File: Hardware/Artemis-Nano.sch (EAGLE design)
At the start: 66 parts, among them J10 USB-C, J11 CORTEX_DEBUG, U2 MCP73831, U3 3.3V, U4 ARTEMIS_MODULESMD, U6 CH340E_MSOP10, Y2 32.768kHz

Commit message: Rename to Nano. Add ignore. Add panel.
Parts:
- removed LOGO2: OSHW-LOGOS, SparkFun-Aesthetics:OSHW-LOGOS
- removed LOGO3: SFE_LOGO_NAME_FLAME.1_INCH, SparkFun-Aesthetics:SFE_LOGO_NAME_FLAME.1_INCH
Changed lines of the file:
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@@
 <grid distance="0.1" unitdist="inch" unit="inch" style="lines" multiple="1" display="no" altdistance="0.01" altunitdist="inch" altunit="inch"/>
 <layers>
-<layer number="1" name="Top" color="4" fill="1" visible="yes" active="no"/>
-<layer number="2" name="Route2" color="16" fill="3" visible="yes" active="no"/>
-<layer number="3" name="Route3" color="4" fill="3" visible="yes" active="no"/>
-<layer number="4" name="Route4" color="1" fill="4" visible="yes" active="no"/>
-<layer number="5" name="Route5" color="4" fill="4" visible="yes" active="no"/>
-<layer number="6" name="Route6" color="1" fill="8" visible="yes" active="no"/>
-<layer number="7" name="Route7" color="4" fill="8" visible="yes" active="no"/>
-<layer number="8" name="Route8" color="1" fill="2" visible="yes" active="no"/>
-<layer number="9" name="Route9" color="4" fill="2" visible="yes" active="no"/>
-<layer number="10" name="Route10" color="1" fill="7" visible="yes" active="no"/>
-<layer number="11" name="Route11" color="4" fill="7" visible="yes" active="no"/>
-<layer number="12" name="Route12" color="1" fill="5" visible="yes" active="no"/>
-<layer number="13" name="Route13" color="4" fill="5" visible="yes" active="no"/>
-<layer number="14" name="Route14" color="1" fill="6" visible="yes" active="no"/>
-<layer number="15" name="Route15" color="23" fill="6" visible="yes" active="no"/>
-<layer number="16" name="Bottom" color="1" fill="1" visible="yes" active="no"/>
-<layer number="17" name="Pads" color="2" fill="1" visible="yes" active="no"/>
-<layer number="18" name="Vias" color="2" fill="1" visible="yes" active="no"/>
-<layer number="19" name="Unrouted" color="6" fill="1" visible="yes" active="no"/>
-<layer number="20" name="Dimension" color="24" fill="1" visible="yes" active="no"/>
-<layer number="21" name="tPlace" color="16" fill="1" visible="yes" active="no"/>
-<layer number="22" name="bPlace" color="14" fill="1" visible="yes" active="no"/>
-<layer number="23" name="tOrigins" color="15" fill="1" visible="yes" active="no"/>
-<layer number="24" name="bOrigins" color="15" fill="1" visible="yes" active="no"/>
-<layer number="25" name="tNames" color="7" fill="1" visible="yes" active="no"/>
-<layer number="26" name="bNames" color="7" fill="1" visible="yes" active="no"/>
-<layer number="27" name="tValues" color="7" fill="1" visible="yes" active="no"/>
-<layer number="28" name="bValues" color="7" fill="1" visible="yes" active="no"/>
+<layer number="1" name="Top" color="4" fill="1" visible="no" active="no"/>
+<layer number="2" name="Route2" color="16" fill="3" visible="no" active="no"/>
+<layer number="3" name="Route3" color="4" fill="3" visible="no" active="no"/>
+<layer number="4" name="Route4" color="1" fill="4" visible="no" active="no"/>
+<layer number="5" name="Route5" color="4" fill="4" visible="no" active="no"/>
+<layer number="6" name="Route6" color="1" fill="8" visible="no" active="no"/>
+<layer number="7" name="Route7" color="4" fill="8" visible="no" active="no"/>
+<layer number="8" name="Route8" color="1" fill="2" visible="no" active="no"/>
+<layer number="9" name="Route9" color="4" fill="2" visible="no" active="no"/>
+<layer number="10" name="Route10" color="1" fill="7" visible="no" active="no"/>
+<layer number="11" name="Route11" color="4" fill="7" visible="no" active="no"/>
+<layer number="12" name="Route12" color="1" fill="5" visible="no" active="no"/>
+<layer number="13" name="Route13" color="4" fill="5" visible="no" active="no"/>
+<layer number="14" name="Route14" color="1" fill="6" visible="no" active="no"/>
+<layer number="15" name="Route15" color="23" fill="6" visible="no" active="no"/>
+<layer number="16" name="Bottom" color="1" fill="1" visible="no" active="no"/>
+<layer number="17" name="Pads" color="2" fill="1" visible="no" active="no"/>
+<layer number="18" name="Vias" color="2" fill="1" visible="no" active="no"/>
+<layer number="19" name="Unrouted" color="6" fill="1" visible="no" active="no"/>
+<layer number="20" name="Dimension" color="24" fill="1" visible="no" active="no"/>
+<layer number="21" name="tPlace" color="16" fill="1" visible="no" active="no"/>
+<layer number="22" name="bPlace" color="14" fill="1" visible="no" active="no"/>
+<layer number="23" name="tOrigins" color="15" fill="1" visible="no" active="no"/>
+<layer number="24" name="bOrigins" color="15" fill="1" visible="no" active="no"/>
+<layer number="25" name="tNames" color="7" fill="1" visible="no" active="no"/>
+<layer number="26" name="bNames" color="7" fill="1" visible="no" active="no"/>
+<layer number="27" name="tValues" color="7" fill="1" visible="no" active="no"/>
+<layer number="28" name="bValues" color="7" fill="1" visible="no" active="no"/>
 <layer number="29" name="tStop" color="7" fill="3" visible="no" active="no"/>
 <layer number="30" name="bStop" color="7" fill="6" visible="no" active="no"/>
@@
 <layer number="35" name="tGlue" color="7" fill="4" visible="no" active="no"/>
 <layer number="36" name="bGlue" color="7" fill="5" visible="no" active="no"/>
-<layer number="37" name="tTest" color="7" fill="1" visible="yes" active="no"/>
-<layer number="38" name="bTest" color="7" fill="1" visible="yes" active="no"/>
+<layer number="37" name="tTest" color="7" fill="1" visible="no" active="no"/>
+<layer number="38" name="bTest" color="7" fill="1" visible="no" active="no"/>
 <layer number="39" name="tKeepout" color="4" fill="11" visible="no" active="no"/>
 <layer number="40" name="bKeepout" color="1" fill="11" visible="no" active="no"/>
@@
 <layer number="44" name="Drills" color="7" fill="1" visible="no" active="no"/>
 <layer number="45" name="Holes" color="7" fill="1" visible="no" active="no"/>
-<layer number="46" name="Milling" color="3" fill="1" visible="yes" active="no"/>
-<layer number="47" name="Measures" color="7" fill="1" visible="yes" active="no"/>
-<layer number="48" name="Document" color="7" fill="1" visible="yes" active="no"/>
-<layer number="49" name="Reference" color="7" fill="1" visible="yes" active="no"/>
-<layer number="50" name="dxf" color="7" fill="1" visible="yes" active="no"/>
-<layer number="51" name="tDocu" color="6" fill="1" visible="yes" active="no"/>
-<layer number="52" name="bDocu" color="7" fill="1" visible="yes" active="no"/>
-<layer number="53" name="tGND_GNDA" color="7" fill="9" visible="yes" active="no"/>
-<layer number="54" name="bGND_GNDA" color="1" fill="9" visible="yes" active="no"/>
-<layer number="56" name="wert" color="7" fill="1" visible="yes" active="no"/>
-<layer number="57" name="tCAD" color="7" fill="1" visible="yes" active="no"/>
-<layer number="59" name="tCarbon" color="7" fill="1" visible="yes" active="no"/>
-<layer number="60" name="bCarbon" color="7" fill="1" visible="yes" active="no"/>
+<layer number="46" name="Milling" color="3" fill="1" visible="no" active="no"/>
+<layer number="47" name="Measures" color="7" fill="1" visible="no" active="no"/>
+<layer number="48" name="Document" color="7" fill="1" visible="no" active="no"/>
+<layer number="49" name="Reference" color="7" fill="1" visible="no" active="no"/>
+<layer number="50" name="dxf" color="7" fill="1" visible="no" active="no"/>
+<layer number="51" name="tDocu" color="6" fill="1" visible="no" active="no"/>
+<layer number="52" name="bDocu" color="7" fill="1" visible="no" active="no"/>
+<layer number="53" name="tGND_GNDA" color="7" fill="9" visible="no" active="no"/>
+<layer number="54" name="bGND_GNDA" color="1" fill="9" visible="no" active="no"/>
+<layer number="56" name="wert" color="7" fill="1" visible="no" active="no"/>
+<layer number="57" name="tCAD" color="7" fill="1" visible="no" active="no"/>
+<layer number="59" name="tCarbon" color="7" fill="1" visible="no" active="no"/>
+<layer number="60" name="bCarbon" color="7" fill="1" visible="no" active="no"/>
 <layer number="88" name="SimResults" color="9" fill="1" visible="yes" active="yes"/>
 <layer number="89" name="SimProbes" color="9" fill="1" visible="yes" active="yes"/>
@@
 <part name="LOGO1" library="SparkFun-Aesthetics" deviceset="SFE_LOGO_FLAME" device=".1_INCH"/>
 <part name="LOGO4" library="SparkFun-Aesthetics" deviceset="SFE_LOGO_FLAME" device=".1_INCH"/>
-<part name="LOGO2" library="SparkFun-Aesthetics" deviceset="OSHW-LOGO" device="S"/>
-<part name="LOGO3" library="SparkFun-Aesthetics" deviceset="SFE_LOGO_NAME_FLAME" device=".1_INCH"/>
 <part name="S1" library="SparkFun-Switches" deviceset="MOMENTARY-SWITCH-SPST" device="-SMD-4.6X2.8MM" value="RESET"/>
 <part name="GND31" library="SparkFun-PowerSymbols" deviceset="GND" device=""/>
@@
 <instance part="LOGO1" gate="G$1" x="75.692" y="10.16" smashed="yes"/>
 <instance part="LOGO4" gate="G$1" x="75.692" y="10.16" smashed="yes"/>
-<instance part="LOGO2" gate="G$1" x="116.84" y="10.16" smashed="yes"/>
-<instance part="LOGO3" gate="G$1" x="43.18" y="-2.54" smashed="yes"/>
 </instances>
 <busses>

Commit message: Fixing PWM pin 7. Updating schematic symbol.
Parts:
- removed U4: ARTEMIS_MODULESMD, Testing:ARTEMIS_MODULESMD
- added U1: ARTEMIS_MODULESMD, Testing:ARTEMIS_MODULESMD
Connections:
- removed net D7/MOSI: J2.4, U4.(MOSI0/CLKOUT)D7
- new net ~D7/MOSI: J2.4, U1.(MOSI0/CLKOUT)~D7
- net !RESET: now also U1.!RST; no longer U4.!RST
- net 3.3V: now also U1.VDD*2; no longer U4.VDD*2
- net BOOT: now also U1.~BOOT(MOSI5/RX1/32KHZ); no longer U4.BOOT(P/MOSI5/RX1/32KHZ)
- net D38: now also U1.(MOSI3/RX1)D38; no longer U4.(MOSI3/RX1)D38
- net D40/RX1: now also U1.(SDA4/MISO4/RX1)D40; no longer U4.(SDA4/MISO4/RX1)D40
- net GND: now also U1.GND*6; no longer U4.GND*6
- net N$2: now also U1.XO; no longer U4.XO
- net N$8: now also U1.XI; no longer U4.XI
- net PDMCLK: now also U1.(TX1/PDMCLK/SCCIO)~D37; no longer U4.(PDMCLK/SCCIO)~D37
- net PDMDATA: now also U1.(RX1/TRIG1/PDMDATA)D36; no longer U4.(RX1/PDMDATA)D36
- net RXI-0: now also U1.~D49(RX0/SDA5/MISO5); no longer U4.RX0(P/SDA5/MISO5)
- net SWDCK: now also U1.D20(SWDCK/TX1); no longer U4.SWDCK
- net SWDIO: now also U1.D21(SWDIO/RX1/SCCRST); no longer U4.SWDIO
- net TXO-0: now also U1.~D48(TX0/SCL5/SCK5); no longer U4.TX0(P/SCL5/SCK5)
- net ~AD11: now also U1.~AD11(PDMDATA); no longer U4.~AD11
- net ~AD12: now also U1.~AD12(PDMCLK/TX1); no longer U4.~AD12
- net ~AD13: now also U1.~AD13(I2SBCLK/RX1); no longer U4.~AD13(I2SCLK)
- net ~AD29: now also U1.~AD29(PDMDATA); no longer U4.~AD29(PDMDATA)
- net ~AD3/SWO: now also U1.~AD33(SWO/32KHZ); no longer U4.~AD33(SWO)
- net ~AD31: now also U1.~AD31(SCCCLK); no longer U4.~AD31(RTS1/SCCLK)
- net ~AD32: now also U1.~AD32(SCCIO); no longer U4.~AD32(SCIO)
- net ~AD35: now also U1.~AD35(TX1/I2SDAT/PDMCLK); no longer U4.~AD35(I2SDAT)
- net ~D18: now also U1.(CMPIN1/SCCIO)~D18; no longer U4.(CMPIN1)~D18
- net ~D19/LED: now also U1.(CMPRF0/SCCCLK/I2SBCLK)~D19; no longer U4.(CMPRF0)~D19
- net ~D22: now also U1.(PDMCLK/SWO)~D22; no longer U4.(PDMCLK)~D22
- net ~D25/SDA2: now also U1.(SDA2/MISO2/RX1)~D25; no longer U4.(SDA2/MISO2/RX1)~D25
- net ~D27/SCL2: now also U1.(SCL2/SCK2)~D27; no longer U4.(SCL2/SCK2)~D27
- net ~D39/TX1: now also U1.(SCL4/SCK4/TX1)~D39; no longer U4.(SCL4/SCK4/TX1)~D39
- net ~D4: now also U1.(RX1/SLINT)~D4; no longer U4.(RX1)~D4
- net ~D42: now also U1.(SCL3/SCK3/TX1)~D42; no longer U4.(SCL3/SCK3/TX1)~D42
- net ~D43: now also U1.(SDA3/MISO3/RX1)~D43; no longer U4.(SDA3/MISO3/RX1)~D43
- net ~D5/SCK: now also U1.(SCL0/SCK0)~D5; no longer U4.(SCL0/SCK0)~D5
- net ~D6/MISO: now also U1.(SDA0/MISO0/I2SDAT)~D6; no longer U4.(SDA0/MISO0/I2SDAT)~D6

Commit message: Fix pin 33 silk
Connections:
- net ~AD3/SWO renamed ~AD33/SWO
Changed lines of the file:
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@@
 </segment>
 </net>
-<net name="~AD3/SWO" class="0">
+<net name="~AD33/SWO" class="0">
 <segment>
 <wire x1="53.34" y1="50.8" x2="50.8" y2="50.8" width="0.1524" layer="91"/>

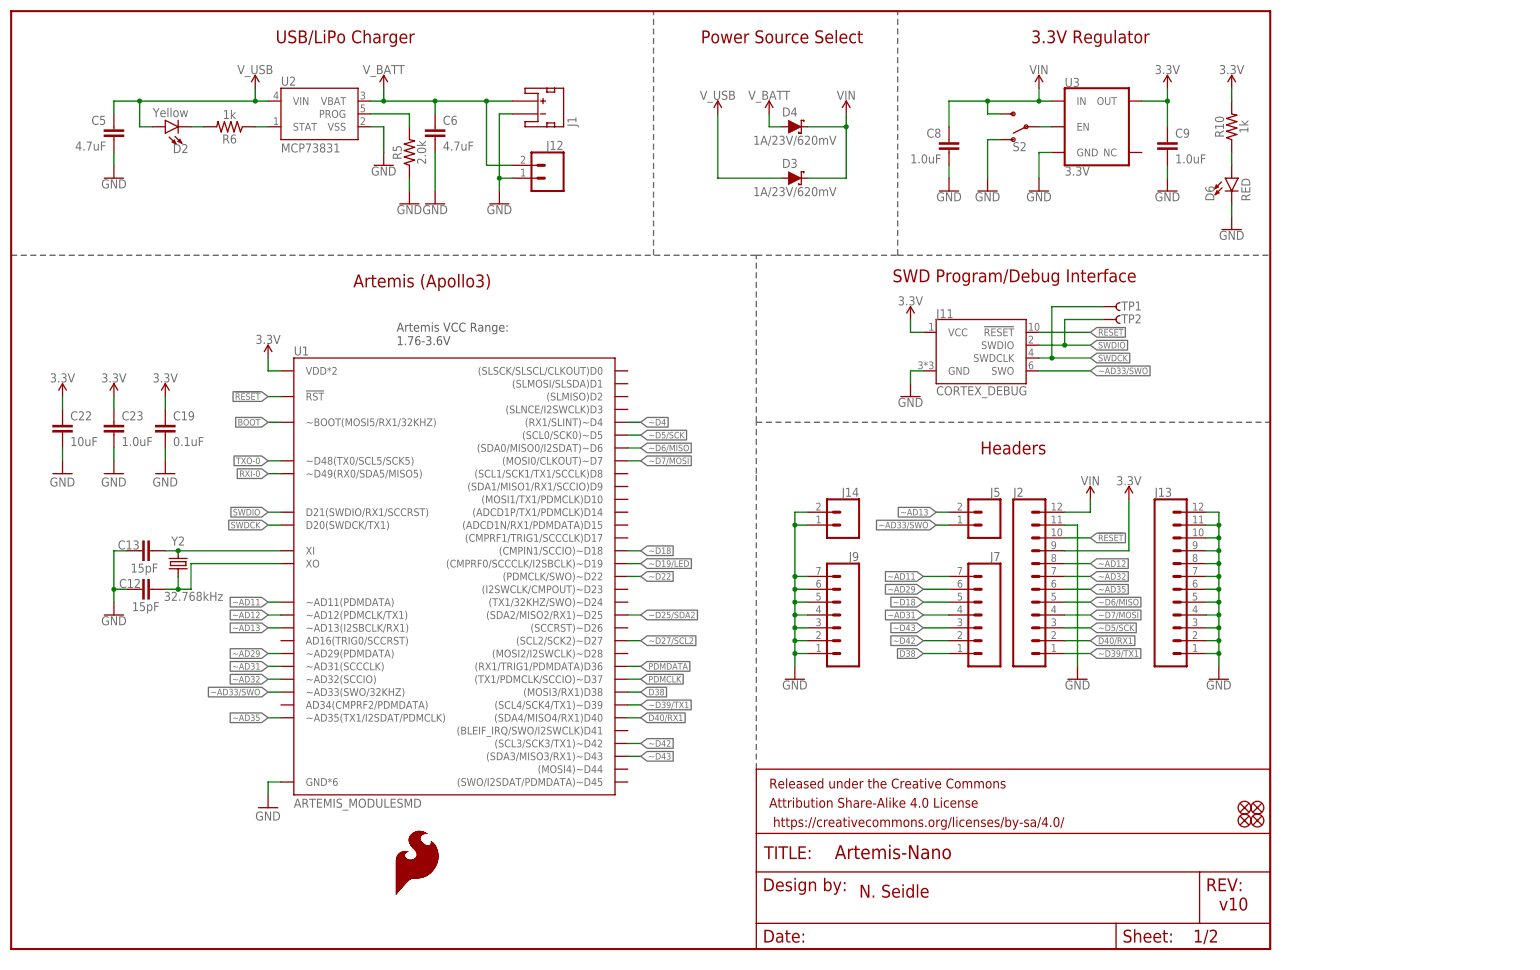
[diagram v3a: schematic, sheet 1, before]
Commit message: Change silk to match new variant
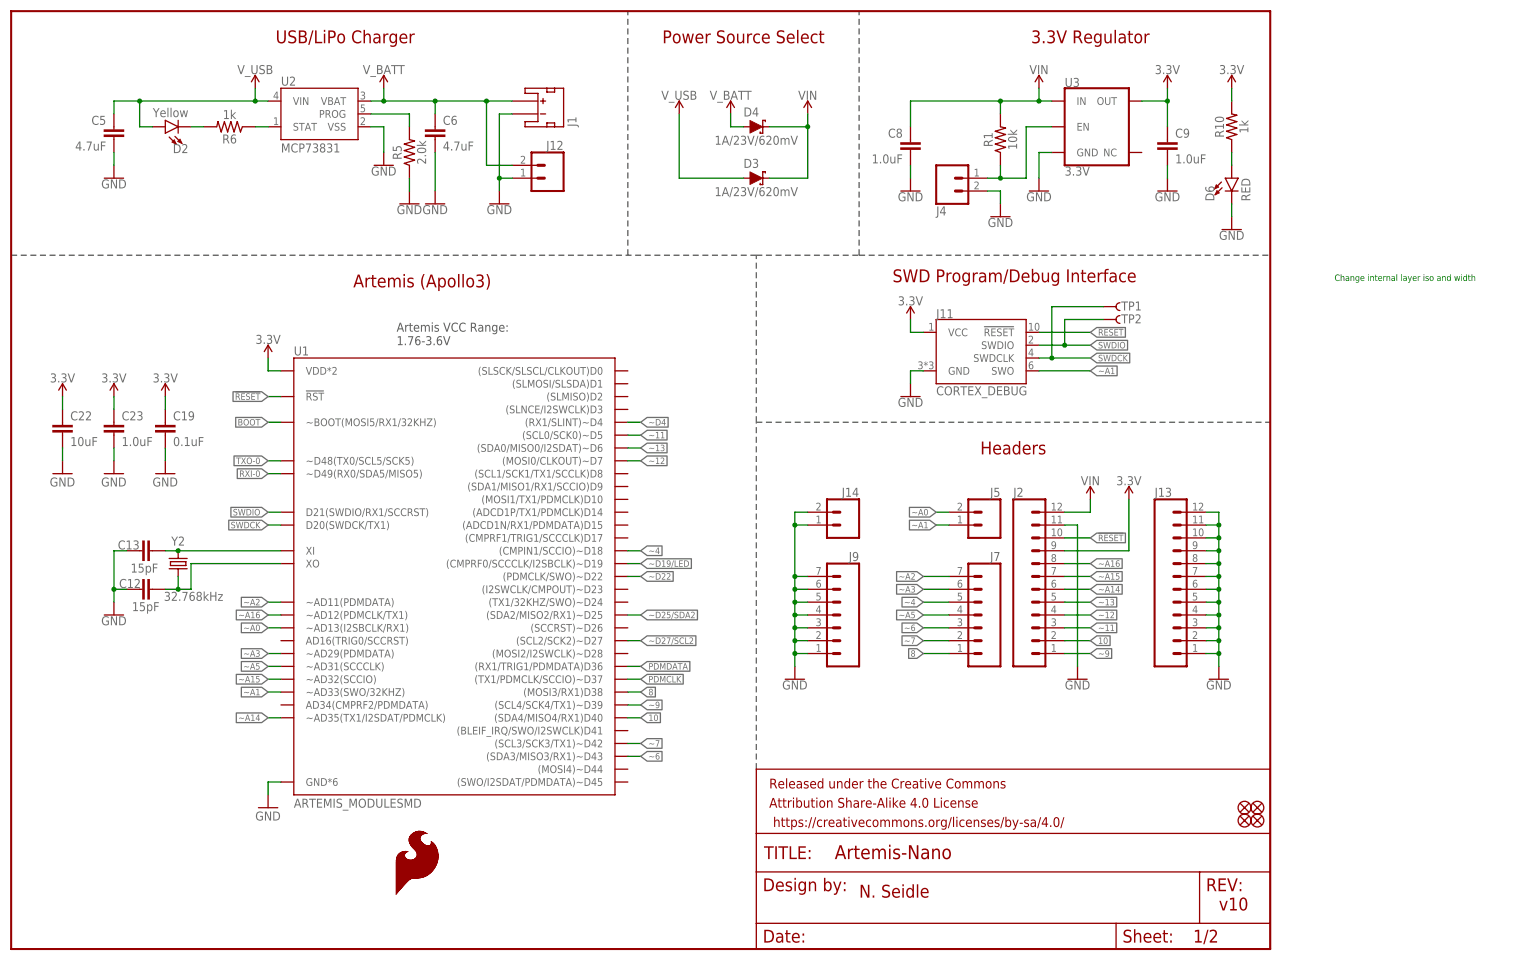
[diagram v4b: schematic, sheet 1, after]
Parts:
- removed S2: (no value), SparkFun-Switches:SWITCH-SPDT-SMD-RIGHT-ANGLE
- added J4: (no value), SparkFun-Connectors:CONN_021X02_NO_SILK
- added R1: 10k, SparkFun-Resistors:10KOHM-0603-1/10W-1%
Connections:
- net D38 renamed 8
- net D40/RX1 renamed 10
- net ~AD11 renamed ~A2
- net ~AD12 renamed ~A16
- net ~AD13 renamed ~A0
- net ~AD29 renamed ~A3
- net ~AD31 renamed ~A5
- net ~AD32 renamed ~A15
- net ~AD33/SWO renamed ~A1
- net ~AD35 renamed ~A14
- net ~D18 renamed ~4
- net ~D39/TX1 renamed ~9
- net ~D42 renamed ~7
- net ~D43 renamed ~6
- net ~D5/SCK renamed ~11
- net ~D6/MISO renamed ~13
- net ~D7/MOSI renamed ~12
- removed net N$6: C17.1, U6.V3
- net 3.3V: now also C17.1, U6.V3
- net GND: now also J4.2; no longer S2.O
- net VIN: now also R1.2; no longer S2.S
- net VREG_EN: now also J4.1, R1.1; no longer S2.P
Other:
- note added: "Change internal layer iso and width"
- moved on the sheet: C8, D3, D4

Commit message: Changing bootload circuit to match what is being shipped. Add ignore.
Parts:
- R12, R16: value 4.7k -> 1k; device SparkFun-Resistors:4.7KOHM-0603-1/10W-1% -> SparkFun-Resistors:1KOHM-0603-1/10W-1%
- R15: value 10k -> 22k; device SparkFun-Resistors:10KOHM-0603-1/10W-1% -> SparkFun-Resistors:22KOHM-0603-1/10W-1%
- R17: value 100k -> DNP; device SparkFun-Resistors:100KOHM-0603-1/10W-1% -> SparkFun-Resistors:1MOHM-0603-1/4W-5%
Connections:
- removed net ~D22: U1.(PDMCLK/SWO)~D22
- removed net ~D4: U1.(RX1/SLINT)~D4
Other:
- note removed: "Change internal layer iso and width"
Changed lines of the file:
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@@
 <?xml version="1.0" encoding="utf-8"?>
 <!DOCTYPE eagle SYSTEM "eagle.dtd">
-<eagle version="9.4.0">
+<eagle version="9.3.0">
 <drawing>
 <settings>
@@
 <part name="GND33" library="SparkFun-PowerSymbols" deviceset="GND" device=""/>
 <part name="D5" library="SparkFun-LED" deviceset="LED-YELLOW" device="0603" value="Yellow"/>
-<part name="R12" library="SparkFun-Resistors" deviceset="4.7KOHM" device="-0603-1/10W-1%" value="4.7k"/>
+<part name="R12" library="SparkFun-Resistors" deviceset="1KOHM" device="-0603-1/10W-1%" value="1k"/>
 <part name="C18" library="SparkFun-Capacitors" deviceset="0.1UF" device="-0603-25V-(+80/-20%)" value="0.1uF"/>
-<part name="R16" library="SparkFun-Resistors" deviceset="4.7KOHM" device="-0603-1/10W-1%" value="4.7k"/>
+<part name="R16" library="SparkFun-Resistors" deviceset="1KOHM" device="-0603-1/10W-1%" value="1k"/>
 <part name="D7" library="SparkFun-LED" deviceset="LED-GREEN" device="0603" value="GREEN"/>
 <part name="J10" library="SparkFun-Connectors" deviceset="USB_C" device="" value="USB-C"/>
@@
 <part name="C20" library="SparkFun-Capacitors" deviceset="0.1UF" device="-0603-25V-5%" value="0.1uF"/>
 <part name="GND41" library="SparkFun-PowerSymbols" deviceset="GND" device=""/>
-<part name="R15" library="SparkFun-Resistors" deviceset="10KOHM" device="-0603-1/10W-1%" value="10k"/>
+<part name="R15" library="SparkFun-Resistors" deviceset="22KOHM" device="-0603-1/10W-1%" value="22k"/>
 <part name="C21" library="SparkFun-Capacitors" deviceset="2.2UF" device="-0603-10V-20%" value="2.2uF"/>
-<part name="R17" library="SparkFun-Resistors" deviceset="100KOHM" device="-0603-1/10W-1%" value="100k"/>
+<part name="R17" library="SparkFun-Resistors" deviceset="1MOHM" device="-0603-1/4W-5%" value="DNP"/>
 <part name="GND44" library="SparkFun-PowerSymbols" deviceset="GND" device=""/>
 <part name="C28" library="SparkFun-Capacitors" deviceset="1.0NF/1000PF" device="-0603-50V-10%" value="1nF"/>
@@
 <text x="76.2" y="119.38" size="1.778" layer="97">Artemis VCC Range:
 1.76-3.6V</text>
-<text x="261.62" y="132.08" size="1.27" layer="91">Change internal layer iso and width</text>
 </plain>
 <instances>
@@
 </segment>
 </net>
-<net name="~D4" class="0">
-<segment>
-<wire x1="121.92" y1="104.14" x2="124.46" y2="104.14" width="0.1524" layer="91"/>
-<label x="124.46" y="104.14" size="1.27" layer="95" xref="yes"/>
-<pinref part="U1" gate="U1" pin="(RX1/SLINT)~D4"/>
-</segment>
-</net>
-<net name="~D22" class="0">
-<segment>
-<wire x1="121.92" y1="73.66" x2="124.46" y2="73.66" width="0.1524" layer="91"/>
-<label x="124.46" y="73.66" size="1.27" layer="95" xref="yes"/>
-<pinref part="U1" gate="U1" pin="(PDMCLK/SWO)~D22"/>
-</segment>
-</net>
